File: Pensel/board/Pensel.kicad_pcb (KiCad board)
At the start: 2 copper layers, 60 x 13 mm, 62 parts, among them J3 JTAG, J4 I2C, J5 UART, P1 USB_PROC, SW2 MAIN, SW3 AUX, SW4 MODE_SEL, U1 STM32F302x6/8, U2 MMA8452Q, U3 MMA8452Q, U4 AP111733

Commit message: further improvements and new export of gerbers
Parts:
- removed the ? at (83.0, 141.1)
- removed the ? at (82.4, 140.5)
- removed the ? at (82.4, 141.1)
- added ?: via-1.0mm, TylerCustom:via-1.0mm, F.Cu at (58.5, 142.3)
- added ?: via-1.0mm, TylerCustom:via-1.0mm, F.Cu at (58.5, 140.8)
- added ?: via-1.0mm, TylerCustom:via-1.0mm, F.Cu at (82.5, 141.1)
- added ?: via-1.0mm, TylerCustom:via-1.0mm, F.Cu at (82.8, 141.1)
- added ?: via-1.0mm, TylerCustom:via-1.0mm, F.Cu at (81.5, 140.8)
- added ?: via-1.0mm, TylerCustom:via-1.0mm, F.Cu at (81.8, 140.8)
- added ?: via-1.0mm, TylerCustom:via-1.0mm, F.Cu at (82.2, 140.8)
- added ?: via-1.0mm, TylerCustom:via-1.0mm, F.Cu at (82.5, 140.8)
- added ?: via-1.0mm, TylerCustom:via-1.0mm, F.Cu at (53.6, 145.5)
- added ?: via-1.0mm, TylerCustom:via-1.0mm, F.Cu at (54.0, 145.5)
- added ?: via-1.0mm, TylerCustom:via-1.0mm, F.Cu at (54.0, 145.1)
- added ?: via-1.0mm, TylerCustom:via-1.0mm, F.Cu at (54.4, 145.1)
- added ?: via-1.0mm, TylerCustom:via-1.0mm, F.Cu at (58.5, 140.4)
- added ?: via-1.0mm, TylerCustom:via-1.0mm, F.Cu at (54.4, 145.5)
- added ?: via-1.0mm, TylerCustom:via-1.0mm, F.Cu at (63.5, 145.8)
- added ?: via-1.0mm, TylerCustom:via-1.0mm, F.Cu at (64.0, 145.8)
- added ?: via-1.0mm, TylerCustom:via-1.0mm, F.Cu at (64.0, 146.2)
- added ?: via-1.0mm, TylerCustom:via-1.0mm, F.Cu at (63.5, 146.2)
- added ?: via-1.0mm, TylerCustom:via-1.0mm, F.Cu at (63.0, 146.2)
- added ?: via-1.0mm, TylerCustom:via-1.0mm, F.Cu at (101.1, 139.8)
- added ?: via-1.0mm, TylerCustom:via-1.0mm, F.Cu at (101.1, 140.2)
- added ?: via-1.0mm, TylerCustom:via-1.0mm, F.Cu at (100.8, 140.2)
- added ?: via-1.0mm, TylerCustom:via-1.0mm, F.Cu at (101.5, 140.2)
- added ?: via-1.0mm, TylerCustom:via-1.0mm, F.Cu at (58.8, 140.4)
- added ?: via-1.0mm, TylerCustom:via-1.0mm, F.Cu at (102.0, 141.5)
- added ?: via-1.0mm, TylerCustom:via-1.0mm, F.Cu at (94.4, 143.3)
- added ?: via-1.0mm, TylerCustom:via-1.0mm, F.Cu at (104.4, 141.8)
- added ?: via-1.0mm, TylerCustom:via-1.0mm, F.Cu at (104.4, 142.3)
- added ?: via-1.0mm, TylerCustom:via-1.0mm, F.Cu at (104.4, 142.8)
- added ?: via-1.0mm, TylerCustom:via-1.0mm, F.Cu at (107.0, 149.5)
- added ?: via-1.0mm, TylerCustom:via-1.0mm, F.Cu at (107.6, 149.5)
- added ?: via-1.0mm, TylerCustom:via-1.0mm, F.Cu at (108.1, 149.5)
- added ?: via-1.0mm, TylerCustom:via-1.0mm, F.Cu at (108.7, 149.5)
- added ?: via-1.0mm, TylerCustom:via-1.0mm, F.Cu at (109.2, 149.5)
- added ?: via-1.0mm, TylerCustom:via-1.0mm, F.Cu at (65.4, 143.7)
- added ?: via-1.0mm, TylerCustom:via-1.0mm, F.Cu at (109.2, 149.9)
- added ?: via-1.0mm, TylerCustom:via-1.0mm, F.Cu at (109.2, 150.4)
- added ?: via-1.0mm, TylerCustom:via-1.0mm, F.Cu at (65.8, 143.3)
- added ?: via-1.0mm, TylerCustom:via-1.0mm, F.Cu at (66.1, 143.3)
- added ?: via-1.0mm, TylerCustom:via-1.0mm, F.Cu at (64.7, 143.3)
- added ?: via-1.0mm, TylerCustom:via-1.0mm, F.Cu at (64.7, 143.7)
- added ?: via-1.0mm, TylerCustom:via-1.0mm, F.Cu at (65.8, 143.7)
- added ?: via-1.0mm, TylerCustom:via-1.0mm, F.Cu at (64.3, 143.3)
- added ?: via-1.0mm, TylerCustom:via-1.0mm, F.Cu at (58.5, 141.2)
- added ?: via-1.0mm, TylerCustom:via-1.0mm, F.Cu at (64.3, 143.7)
- added ?: via-1.0mm, TylerCustom:via-1.0mm, F.Cu at (65.0, 143.7)
- added ?: via-1.0mm, TylerCustom:via-1.0mm, F.Cu at (65.0, 143.3)
- added ?: via-1.0mm, TylerCustom:via-1.0mm, F.Cu at (65.4, 143.3)
- added ?: via-1.0mm, TylerCustom:via-1.0mm, F.Cu at (66.1, 143.7)
- added ?: via-1.0mm, TylerCustom:via-1.0mm, F.Cu at (68.0, 140.1)
- added ?: via-1.0mm, TylerCustom:via-1.0mm, F.Cu at (68.0, 140.4)
- added ?: via-1.0mm, TylerCustom:via-1.0mm, F.Cu at (67.6, 140.1)
- added ?: via-1.0mm, TylerCustom:via-1.0mm, F.Cu at (67.6, 140.4)
- added ?: via-1.0mm, TylerCustom:via-1.0mm, F.Cu at (68.3, 140.4)
- added ?: via-1.0mm, TylerCustom:via-1.0mm, F.Cu at (58.5, 141.9)
- added ?: via-1.0mm, TylerCustom:via-1.0mm, F.Cu at (68.3, 140.1)
- added ?: via-1.0mm, TylerCustom:via-1.0mm, F.Cu at (66.8, 140.1)
- added ?: via-1.0mm, TylerCustom:via-1.0mm, F.Cu at (66.8, 140.4)
- added ?: via-1.0mm, TylerCustom:via-1.0mm, F.Cu at (67.2, 140.4)
- added ?: via-1.0mm, TylerCustom:via-1.0mm, F.Cu at (67.2, 140.1)
- added ?: via-1.0mm, TylerCustom:via-1.0mm, F.Cu at (66.5, 140.4)
- added ?: via-1.0mm, TylerCustom:via-1.0mm, F.Cu at (66.5, 140.1)
- added ?: via-1.0mm, TylerCustom:via-1.0mm, F.Cu at (73.8, 142.8)
- added ?: via-1.0mm, TylerCustom:via-1.0mm, F.Cu at (73.1, 142.1)
- added ?: via-1.0mm, TylerCustom:via-1.0mm, F.Cu at (73.5, 143.2)
- added ?: via-1.0mm, TylerCustom:via-1.0mm, F.Cu at (58.8, 141.9)
- added ?: via-1.0mm, TylerCustom:via-1.0mm, F.Cu at (73.8, 143.2)
- added ?: via-1.0mm, TylerCustom:via-1.0mm, F.Cu at (73.5, 142.1)
- added ?: via-1.0mm, TylerCustom:via-1.0mm, F.Cu at (73.8, 142.1)
- added ?: via-1.0mm, TylerCustom:via-1.0mm, F.Cu at (73.1, 143.2)
- added ?: via-1.0mm, TylerCustom:via-1.0mm, F.Cu at (73.8, 143.5)
- added ?: via-1.0mm, TylerCustom:via-1.0mm, F.Cu at (73.1, 143.5)
- added ?: via-1.0mm, TylerCustom:via-1.0mm, F.Cu at (73.5, 143.5)
- added ?: via-1.0mm, TylerCustom:via-1.0mm, F.Cu at (73.8, 142.4)
- added ?: via-1.0mm, TylerCustom:via-1.0mm, F.Cu at (73.1, 142.8)
- added ?: via-1.0mm, TylerCustom:via-1.0mm, F.Cu at (73.5, 142.8)
- added ?: via-1.0mm, TylerCustom:via-1.0mm, F.Cu at (58.8, 140.8)
- added ?: via-1.0mm, TylerCustom:via-1.0mm, F.Cu at (73.1, 142.4)
- added ?: via-1.0mm, TylerCustom:via-1.0mm, F.Cu at (73.5, 142.4)
- added ?: via-1.0mm, TylerCustom:via-1.0mm, F.Cu at (91.8, 143.8)
- added ?: via-1.0mm, TylerCustom:via-1.0mm, F.Cu at (98.9, 143.8)
- added ?: via-1.0mm, TylerCustom:via-1.0mm, F.Cu at (98.2, 143.8)
- added ?: via-1.0mm, TylerCustom:via-1.0mm, F.Cu at (98.9, 143.4)
- added ?: via-1.0mm, TylerCustom:via-1.0mm, F.Cu at (99.7, 143.4)
- added ?: via-1.0mm, TylerCustom:via-1.0mm, F.Cu at (98.2, 143.4)
- added ?: via-1.0mm, TylerCustom:via-1.0mm, F.Cu at (98.9, 143.1)
- added ?: via-1.0mm, TylerCustom:via-1.0mm, F.Cu at (99.7, 143.1)
- added ?: via-1.0mm, TylerCustom:via-1.0mm, F.Cu at (58.8, 141.6)
- added ?: via-1.0mm, TylerCustom:via-1.0mm, F.Cu at (98.2, 143.1)
- added ?: via-1.0mm, TylerCustom:via-1.0mm, F.Cu at (98.9, 142.8)
- added ?: via-1.0mm, TylerCustom:via-1.0mm, F.Cu at (99.7, 142.8)
- added ?: via-1.0mm, TylerCustom:via-1.0mm, F.Cu at (98.2, 142.8)
- added ?: via-1.0mm, TylerCustom:via-1.0mm, F.Cu at (98.9, 142.4)
- added ?: via-1.0mm, TylerCustom:via-1.0mm, F.Cu at (99.7, 142.4)
- added ?: via-1.0mm, TylerCustom:via-1.0mm, F.Cu at (98.2, 142.4)
- added ?: via-1.0mm, TylerCustom:via-1.0mm, F.Cu at (98.9, 142.1)
- added ?: via-1.0mm, TylerCustom:via-1.0mm, F.Cu at (99.7, 142.1)
- added ?: via-1.0mm, TylerCustom:via-1.0mm, F.Cu at (98.2, 142.1)
- added ?: via-1.0mm, TylerCustom:via-1.0mm, F.Cu at (58.8, 142.3)
- added ?: via-1.0mm, TylerCustom:via-1.0mm, F.Cu at (98.9, 141.7)
- added ?: via-1.0mm, TylerCustom:via-1.0mm, F.Cu at (99.7, 141.7)
- added ?: via-1.0mm, TylerCustom:via-1.0mm, F.Cu at (98.2, 141.7)
- added ?: via-1.0mm, TylerCustom:via-1.0mm, F.Cu at (98.9, 141.3)
- added ?: via-1.0mm, TylerCustom:via-1.0mm, F.Cu at (99.7, 141.3)
- added ?: via-1.0mm, TylerCustom:via-1.0mm, F.Cu at (98.2, 141.3)
- added ?: via-1.0mm, TylerCustom:via-1.0mm, F.Cu at (98.9, 141.0)
- added ?: via-1.0mm, TylerCustom:via-1.0mm, F.Cu at (99.7, 141.0)
- added ?: via-1.0mm, TylerCustom:via-1.0mm, F.Cu at (98.2, 141.0)
- added ?: via-1.0mm, TylerCustom:via-1.0mm, F.Cu at (98.9, 140.7)
- added ?: via-1.0mm, TylerCustom:via-1.0mm, F.Cu at (58.5, 141.6)
- added ?: via-1.0mm, TylerCustom:via-1.0mm, F.Cu at (99.7, 140.7)
- added ?: via-1.0mm, TylerCustom:via-1.0mm, F.Cu at (98.2, 140.7)
- added ?: via-1.0mm, TylerCustom:via-1.0mm, F.Cu at (81.5, 142.2)
- added ?: via-1.0mm, TylerCustom:via-1.0mm, F.Cu at (81.8, 142.2)
- added ?: via-1.0mm, TylerCustom:via-1.0mm, F.Cu at (82.2, 142.2)
- added ?: via-1.0mm, TylerCustom:via-1.0mm, F.Cu at (82.5, 142.2)
- added ?: via-1.0mm, TylerCustom:via-1.0mm, F.Cu at (82.8, 142.2)
- added ?: via-1.0mm, TylerCustom:via-1.0mm, F.Cu at (81.5, 141.8)
- added ?: via-1.0mm, TylerCustom:via-1.0mm, F.Cu at (81.8, 141.8)
- added ?: via-1.0mm, TylerCustom:via-1.0mm, F.Cu at (82.2, 141.8)
- added ?: via-1.0mm, TylerCustom:via-1.0mm, F.Cu at (58.8, 141.2)
- added ?: via-1.0mm, TylerCustom:via-1.0mm, F.Cu at (82.5, 141.8)
- added ?: via-1.0mm, TylerCustom:via-1.0mm, F.Cu at (82.8, 141.8)
- added ?: via-1.0mm, TylerCustom:via-1.0mm, F.Cu at (81.5, 141.4)
- added ?: via-1.0mm, TylerCustom:via-1.0mm, F.Cu at (81.8, 141.4)
- added ?: via-1.0mm, TylerCustom:via-1.0mm, F.Cu at (82.2, 141.4)
- added ?: via-1.0mm, TylerCustom:via-1.0mm, F.Cu at (82.5, 141.4)
- added ?: via-1.0mm, TylerCustom:via-1.0mm, F.Cu at (82.8, 141.4)
- added ?: via-1.0mm, TylerCustom:via-1.0mm, F.Cu at (81.5, 141.1)
- added ?: via-1.0mm, TylerCustom:via-1.0mm, F.Cu at (81.8, 141.1)
- added ?: via-1.0mm, TylerCustom:via-1.0mm, F.Cu at (82.2, 141.1)
- added REF**: Fiducial_1mm_Dia_2.54mm_Outer_CopperTop, Fiducials:Fiducial_1mm_Dia_2.54mm_Outer_CopperTop, B.Cu at (107.2, 139.7)
- added REF**: Fiducial_1mm_Dia_2.54mm_Outer_CopperTop, Fiducials:Fiducial_1mm_Dia_2.54mm_Outer_CopperTop, B.Cu at (52.0, 149.4)
- moved C10 8.43 mm to (107.8, 150.3), turned to 0 degrees
- moved ? 4.52 mm to (102.0, 141.0)
- moved ? 4.31 mm to (102.0, 142.0)
- moved ? 3.22 mm to (104.4, 141.4)
- moved C11 1.77 mm to (107.5, 146.0)
- moved C5 1.48 mm to (92.0, 141.9), turned to 270 degrees
- moved C7 1.48 mm to (90.8, 141.9), turned to 270 degrees
- moved ? 1.05 mm to (92.6, 143.8)
- moved REF** 0.78 mm to (103.4, 139.9)
- moved R3 0.71 mm to (95.5, 141.2), turned to 315 degrees
- moved ? 0.39 mm to (94.7, 143.6)
- moved R17 0.36 mm to (98.0, 147.1)
- moved ? 0.29 mm to (82.8, 140.8)
- moved ? 0.18 mm to (95.0, 143.9)
- moved ? 0.08 mm to (92.2, 143.5)
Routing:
- net +3V3: track 94.1 -> 90.1 mm, vias 19 -> 15
- net +5V: track 8.02 -> 9.43 mm
- net (no net): track 0.00 -> 0.70 mm
- net SWDIO: track 17.6 -> 17.0 mm
- net RESET_n: track 44.8 -> 44.2 mm
- net SWD-SWCLK: track 17.0 -> 16.3 mm
- net SWD-SWO: track 16.0 -> 15.4 mm
- net GND: track 68.2 -> 67.7 mm
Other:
- board text added: "1.0 3/17 Tyler Holmes"
- board text added: "GND"
- board text added: "I2C"
- board text added: "Pensel"
- board text added: "RX"
- board text added: "SCL"
- board text added: "SDA"
- board text added: "TX"
- board text added: "UART"

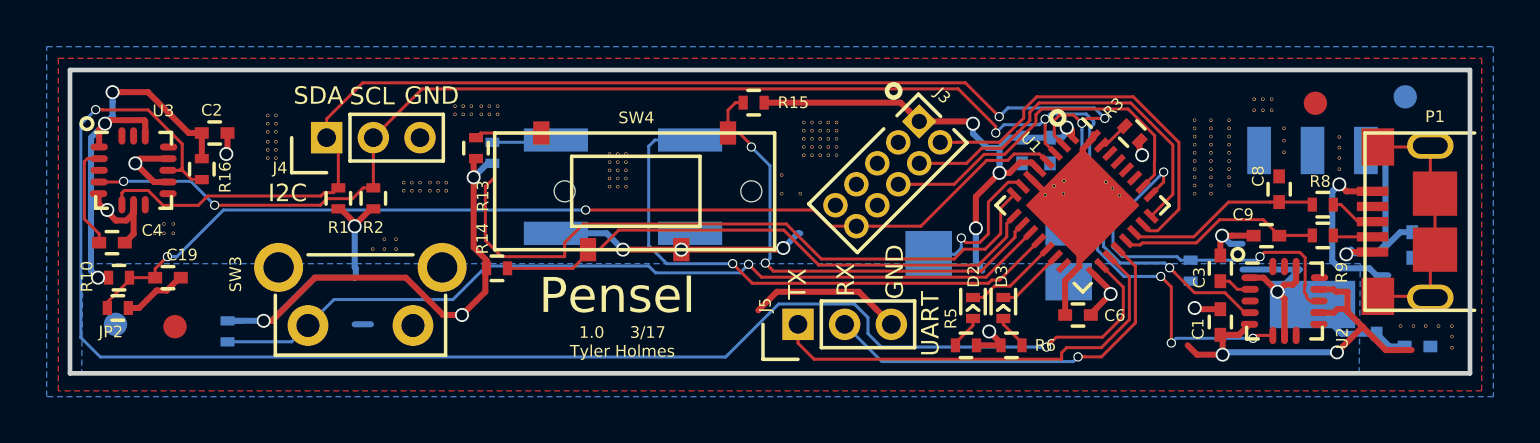
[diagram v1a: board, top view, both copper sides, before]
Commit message: switched to LSM303DLHC accel and gyro only and did first cut at ull route
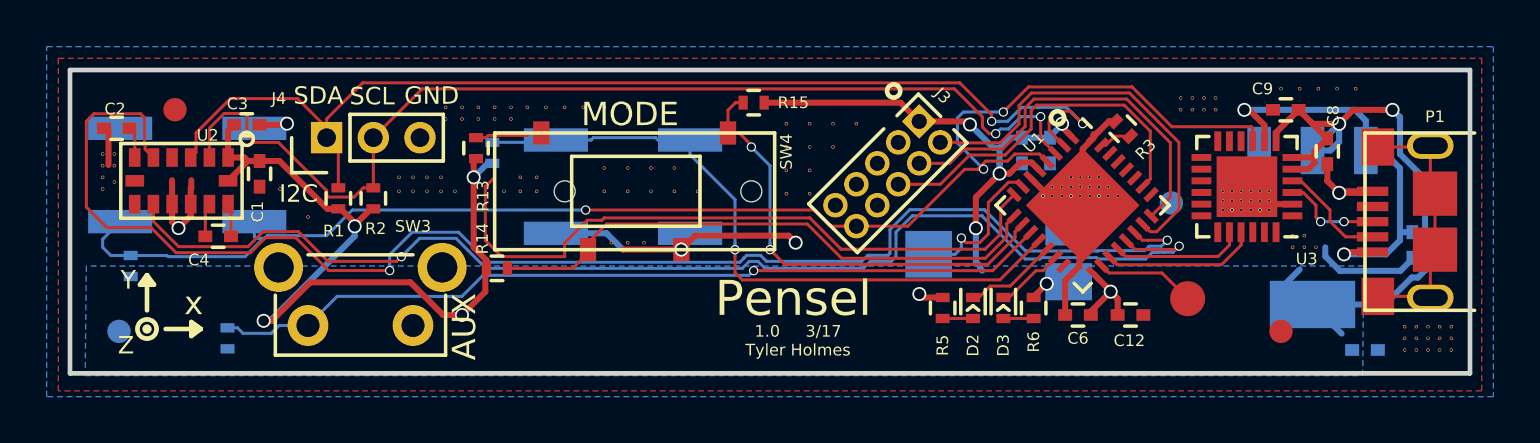
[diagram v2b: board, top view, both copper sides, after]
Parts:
- removed the ? at (58.5, 142.3)
- removed the ? at (58.5, 140.8)
- removed the ? at (82.5, 141.1)
- removed the ? at (82.8, 141.1)
- removed the ? at (81.5, 140.8)
- removed the ? at (81.8, 140.8)
- removed the ? at (82.2, 140.8)
- removed the ? at (82.5, 140.8)
- removed the ? at (53.6, 145.5)
- removed the ? at (54.0, 145.5)
- removed the ? at (54.0, 145.1)
- removed the ? at (54.4, 145.1)
- removed the ? at (58.5, 140.4)
- removed the ? at (54.4, 145.5)
- removed the ? at (63.5, 145.8)
- removed the ? at (64.0, 145.8)
- removed the ? at (64.0, 146.2)
- removed the ? at (63.5, 146.2)
- removed the ? at (63.0, 146.2)
- removed the ? at (101.1, 139.8)
- removed the ? at (101.1, 140.2)
- removed the ? at (100.8, 140.2)
- removed the ? at (101.5, 140.2)
- removed the ? at (58.8, 140.4)
- removed the ? at (102.0, 141.5)
- removed the ? at (94.4, 143.3)
- removed the ? at (104.4, 141.8)
- removed the ? at (104.4, 142.3)
- removed the ? at (104.4, 142.8)
- removed the ? at (107.0, 149.5)
- removed the ? at (107.6, 149.5)
- removed the ? at (108.1, 149.5)
- removed the ? at (108.7, 149.5)
- removed the ? at (109.2, 149.5)
- removed the ? at (65.4, 143.7)
- removed the ? at (109.2, 149.9)
- removed the ? at (109.2, 150.4)
- removed the ? at (94.7, 143.6)
- removed the ? at (82.8, 140.8)
- removed the ? at (95.0, 143.9)
- removed the ? at (104.4, 141.4)
- removed the ? at (101.5, 139.8)
- removed the ? at (100.8, 139.8)
- removed the ? at (81.3, 143.8)
- removed the ? at (80.5, 143.0)
- removed the ? at (65.8, 143.3)
- removed the ? at (80.5, 143.8)
- removed the ? at (92.6, 143.8)
- removed the ? at (92.6, 143.2)
- removed the ? at (92.2, 143.5)
- removed the ? at (102.0, 141.0)
- removed the ? at (102.0, 142.0)
- removed the ? at (66.1, 143.3)
- removed the ? at (64.7, 143.3)
- removed the ? at (64.7, 143.7)
- removed the ? at (65.8, 143.7)
- removed the ? at (64.3, 143.3)
- removed the ? at (58.5, 141.2)
- removed the ? at (64.3, 143.7)
- removed the ? at (65.0, 143.7)
- removed the ? at (65.0, 143.3)
- removed the ? at (65.4, 143.3)
- removed the ? at (66.1, 143.7)
- removed the ? at (68.0, 140.1)
- removed the ? at (68.0, 140.4)
- removed the ? at (67.6, 140.1)
- removed the ? at (67.6, 140.4)
- removed the ? at (68.3, 140.4)
- removed the ? at (58.5, 141.9)
- removed the ? at (68.3, 140.1)
- removed the ? at (66.8, 140.1)
- removed the ? at (66.8, 140.4)
- removed the ? at (67.2, 140.4)
- removed the ? at (67.2, 140.1)
- removed the ? at (66.5, 140.4)
- removed the ? at (66.5, 140.1)
- removed the ? at (73.8, 142.8)
- removed the ? at (73.1, 142.1)
- removed the ? at (73.5, 143.2)
- removed the ? at (58.8, 141.9)
- removed the ? at (73.8, 143.2)
- removed the ? at (73.5, 142.1)
- removed the ? at (73.8, 142.1)
- removed the ? at (73.1, 143.2)
- removed the ? at (73.8, 143.5)
- removed the ? at (73.1, 143.5)
- removed the ? at (73.5, 143.5)
- removed the ? at (73.8, 142.4)
- removed the ? at (73.1, 142.8)
- removed the ? at (73.5, 142.8)
- removed the ? at (58.8, 140.8)
- removed the ? at (73.1, 142.4)
- removed the ? at (73.5, 142.4)
- removed the ? at (91.8, 143.8)
- removed the ? at (98.9, 143.8)
- removed the ? at (98.2, 143.8)
- removed the ? at (98.9, 143.4)
- removed the ? at (99.7, 143.4)
- removed the ? at (98.2, 143.4)
- removed the ? at (98.9, 143.1)
- removed the ? at (99.7, 143.1)
- removed the ? at (58.8, 141.6)
- removed the ? at (98.2, 143.1)
- removed the ? at (98.9, 142.8)
- removed the ? at (99.7, 142.8)
- removed the ? at (98.2, 142.8)
- removed the ? at (98.9, 142.4)
- removed the ? at (99.7, 142.4)
- removed the ? at (98.2, 142.4)
- removed the ? at (98.9, 142.1)
- removed the ? at (99.7, 142.1)
- removed the ? at (98.2, 142.1)
- removed the ? at (58.8, 142.3)
- removed the ? at (98.9, 141.7)
- removed the ? at (99.7, 141.7)
- removed the ? at (98.2, 141.7)
- removed the ? at (98.9, 141.3)
- removed the ? at (99.7, 141.3)
- removed the ? at (98.2, 141.3)
- removed the ? at (98.9, 141.0)
- removed the ? at (99.7, 141.0)
- removed the ? at (98.2, 141.0)
- removed the ? at (98.9, 140.7)
- removed the ? at (58.5, 141.6)
- removed the ? at (99.7, 140.7)
- removed the ? at (98.2, 140.7)
- removed the ? at (81.5, 142.2)
- removed the ? at (81.8, 142.2)
- removed the ? at (82.2, 142.2)
- removed the ? at (82.5, 142.2)
- removed the ? at (82.8, 142.2)
- removed the ? at (81.5, 141.8)
- removed the ? at (81.8, 141.8)
- removed the ? at (82.2, 141.8)
- removed the ? at (58.8, 141.2)
- removed the ? at (82.5, 141.8)
- removed the ? at (82.8, 141.8)
- removed the ? at (81.5, 141.4)
- removed the ? at (81.8, 141.4)
- removed the ? at (82.2, 141.4)
- removed the ? at (82.5, 141.4)
- removed the ? at (82.8, 141.4)
- removed the ? at (81.5, 141.1)
- removed the ? at (81.8, 141.1)
- removed the ? at (82.2, 141.1)
- removed C15, C19: 0.1 uF, Capacitors_SMD:C_0402
- removed JP2: JMPR, Resistors_SMD:R_0402
- removed R16, R17: 4K7, Resistors_SMD:R_0402
- removed R8, R9: 27R, Resistors_SMD:R_0402
- removed REF** (x4): Fiducial_1mm_Dia_2.54mm_Outer_CopperTop, Fiducials:Fiducial_1mm_Dia_2.54mm_Outer_CopperTop
- added ?: via-1.0mm, TylerCustom:via-1.0mm, F.Cu at (83.7, 140.8)
- added ?: via-1.0mm, TylerCustom:via-1.0mm, F.Cu at (66.8, 140.1)
- added ?: via-1.0mm, TylerCustom:via-1.0mm, F.Cu at (92.5, 143.5)
- added ?: via-1.0mm, TylerCustom:via-1.0mm, F.Cu at (92.9, 143.5)
- added ?: via-1.0mm, TylerCustom:via-1.0mm, F.Cu at (93.3, 143.5)
- added ?: via-1.0mm, TylerCustom:via-1.0mm, F.Cu at (93.7, 143.5)
- added ?: via-1.0mm, TylerCustom:via-1.0mm, F.Cu at (94.1, 143.5)
- added ?: via-1.0mm, TylerCustom:via-1.0mm, F.Cu at (94.5, 143.5)
- added ?: via-1.0mm, TylerCustom:via-1.0mm, F.Cu at (94.9, 143.9)
- added ?: via-1.0mm, TylerCustom:via-1.0mm, F.Cu at (94.5, 143.9)
- added ?: via-1.0mm, TylerCustom:via-1.0mm, F.Cu at (94.1, 143.9)
- added ?: via-1.0mm, TylerCustom:via-1.0mm, F.Cu at (93.7, 143.9)
- added ?: via-1.0mm, TylerCustom:via-1.0mm, F.Cu at (67.5, 140.1)
- added ?: via-1.0mm, TylerCustom:via-1.0mm, F.Cu at (93.3, 143.9)
- added ?: via-1.0mm, TylerCustom:via-1.0mm, F.Cu at (92.9, 143.9)
- added ?: via-1.0mm, TylerCustom:via-1.0mm, F.Cu at (92.5, 143.9)
- added ?: via-1.0mm, TylerCustom:via-1.0mm, F.Cu at (92.1, 143.9)
- added ?: via-1.0mm, TylerCustom:via-1.0mm, F.Cu at (91.7, 143.9)
- added ?: via-1.0mm, TylerCustom:via-1.0mm, F.Cu at (101.4, 143.7)
- added ?: via-1.0mm, TylerCustom:via-1.0mm, F.Cu at (101.0, 143.7)
- added ?: via-1.0mm, TylerCustom:via-1.0mm, F.Cu at (100.6, 143.7)
- added ?: via-1.0mm, TylerCustom:via-1.0mm, F.Cu at (100.2, 143.7)
- added ?: via-1.0mm, TylerCustom:via-1.0mm, F.Cu at (99.8, 143.7)
- added ?: via-1.0mm, TylerCustom:via-1.0mm, F.Cu at (68.2, 140.1)
- added ?: via-1.0mm, TylerCustom:via-1.0mm, F.Cu at (99.4, 143.7)
- added ?: via-1.0mm, TylerCustom:via-1.0mm, F.Cu at (99.4, 144.1)
- added ?: via-1.0mm, TylerCustom:via-1.0mm, F.Cu at (99.8, 144.1)
- added ?: via-1.0mm, TylerCustom:via-1.0mm, F.Cu at (100.2, 144.1)
- added ?: via-1.0mm, TylerCustom:via-1.0mm, F.Cu at (100.6, 144.1)
- added ?: via-1.0mm, TylerCustom:via-1.0mm, F.Cu at (101.0, 144.1)
- added ?: via-1.0mm, TylerCustom:via-1.0mm, F.Cu at (101.4, 144.1)
- added ?: via-1.0mm, TylerCustom:via-1.0mm, F.Cu at (101.4, 144.5)
- added ?: via-1.0mm, TylerCustom:via-1.0mm, F.Cu at (101.0, 144.5)
- added ?: via-1.0mm, TylerCustom:via-1.0mm, F.Cu at (100.6, 144.5)
- added ?: via-1.0mm, TylerCustom:via-1.0mm, F.Cu at (68.9, 140.1)
- added ?: via-1.0mm, TylerCustom:via-1.0mm, F.Cu at (100.2, 144.5)
- added ?: via-1.0mm, TylerCustom:via-1.0mm, F.Cu at (99.8, 144.5)
- added ?: via-1.0mm, TylerCustom:via-1.0mm, F.Cu at (99.4, 144.5)
- added ?: via-1.0mm, TylerCustom:via-1.0mm, F.Cu at (109.2, 149.5)
- added ?: via-1.0mm, TylerCustom:via-1.0mm, B.Cu at (108.7, 149.5)
- added ?: via-1.0mm, TylerCustom:via-1.0mm, F.Cu at (108.2, 149.5)
- added ?: via-1.0mm, TylerCustom:via-1.0mm, F.Cu at (69.6, 140.1)
- added ?: via-1.0mm, TylerCustom:via-1.0mm, F.Cu at (70.4, 140.1)
- added ?: via-1.0mm, TylerCustom:via-1.0mm, F.Cu at (71.2, 140.1)
- added ?: via-1.0mm, TylerCustom:via-1.0mm, F.Cu at (72.0, 140.1)
- added ?: via-1.0mm, TylerCustom:via-1.0mm, F.Cu at (70.0, 143.1)
- added ?: via-1.0mm, TylerCustom:via-1.0mm, F.Cu at (69.3, 143.1)
- added ?: via-1.0mm, TylerCustom:via-1.0mm, F.Cu at (82.7, 140.8)
- added ?: via-1.0mm, TylerCustom:via-1.0mm, F.Cu at (68.6, 143.7)
- added ?: via-1.0mm, TylerCustom:via-1.0mm, F.Cu at (69.3, 143.7)
- added ?: via-1.0mm, TylerCustom:via-1.0mm, F.Cu at (70.0, 143.7)
- added ?: via-1.0mm, TylerCustom:via-1.0mm, F.Cu at (59.0, 143.6)
- added ?: via-1.0mm, TylerCustom:via-1.0mm, F.Cu at (64.1, 143.1)
- added ?: via-1.0mm, TylerCustom:via-1.0mm, F.Cu at (64.7, 143.1)
- added ?: via-1.0mm, TylerCustom:via-1.0mm, F.Cu at (65.3, 143.1)
- added ?: via-1.0mm, TylerCustom:via-1.0mm, F.Cu at (65.9, 143.1)
- added ?: via-1.0mm, TylerCustom:via-1.0mm, F.Cu at (66.5, 143.7)
- added ?: via-1.0mm, TylerCustom:via-1.0mm, F.Cu at (65.9, 143.7)
- added ?: via-1.0mm, TylerCustom:via-1.0mm, F.Cu at (82.7, 141.8)
- added ?: via-1.0mm, TylerCustom:via-1.0mm, F.Cu at (65.3, 143.7)
- added ?: via-1.0mm, TylerCustom:via-1.0mm, F.Cu at (64.7, 143.7)
- added ?: via-1.0mm, TylerCustom:via-1.0mm, F.Cu at (64.1, 143.7)
- added ?: via-1.0mm, TylerCustom:via-1.0mm, F.Cu at (74.6, 145.9)
- added ?: via-1.0mm, TylerCustom:via-1.0mm, F.Cu at (73.9, 145.9)
- added ?: via-1.0mm, TylerCustom:via-1.0mm, F.Cu at (73.2, 145.9)
- added ?: via-1.0mm, TylerCustom:via-1.0mm, F.Cu at (105.1, 139.3)
- added ?: via-1.0mm, TylerCustom:via-1.0mm, F.Cu at (102.9, 145.6)
- added ?: via-1.0mm, TylerCustom:via-1.0mm, F.Cu at (102.4, 145.6)
- added ?: via-1.0mm, TylerCustom:via-1.0mm, F.Cu at (102.4, 146.1)
- added ?: via-1.0mm, TylerCustom:via-1.0mm, F.Cu at (68.9, 140.6)
- added ?: via-1.0mm, TylerCustom:via-1.0mm, F.Cu at (102.9, 146.1)
- added ?: via-1.0mm, TylerCustom:via-1.0mm, F.Cu at (103.4, 146.1)
- added ?: via-1.0mm, TylerCustom:via-1.0mm, F.Cu at (107.2, 150.5)
- added ?: via-1.0mm, TylerCustom:via-1.0mm, F.Cu at (107.7, 150.5)
- added ?: via-1.0mm, TylerCustom:via-1.0mm, F.Cu at (108.2, 150.5)
- added ?: via-1.0mm, TylerCustom:via-1.0mm, F.Cu at (108.7, 150.5)
- added ?: via-1.0mm, TylerCustom:via-1.0mm, F.Cu at (109.2, 150.5)
- added ?: via-1.0mm, TylerCustom:via-1.0mm, F.Cu at (109.2, 150.0)
- added ?: via-1.0mm, TylerCustom:via-1.0mm, F.Cu at (108.7, 150.0)
- added ?: via-1.0mm, TylerCustom:via-1.0mm, F.Cu at (108.2, 150.0)
- added ?: via-1.0mm, TylerCustom:via-1.0mm, F.Cu at (68.2, 140.6)
- added ?: via-1.0mm, TylerCustom:via-1.0mm, F.Cu at (107.7, 150.0)
- added ?: via-1.0mm, TylerCustom:via-1.0mm, F.Cu at (107.2, 150.0)
- added ?: via-1.0mm, TylerCustom:via-1.0mm, F.Cu at (107.2, 149.5)
- added ?: via-1.0mm, TylerCustom:via-1.0mm, F.Cu at (107.7, 149.5)
- added ?: via-1.0mm, TylerCustom:via-1.0mm, F.Cu at (73.9, 140.1)
- added ?: via-1.0mm, TylerCustom:via-1.0mm, F.Cu at (72.9, 140.1)
- added ?: via-1.0mm, TylerCustom:via-1.0mm, F.Cu at (73.9, 140.7)
- added ?: via-1.0mm, TylerCustom:via-1.0mm, F.Cu at (81.7, 140.8)
- added ?: via-1.0mm, TylerCustom:via-1.0mm, F.Cu at (80.7, 140.8)
- added ?: via-1.0mm, TylerCustom:via-1.0mm, F.Cu at (81.7, 141.8)
- added ?: via-1.0mm, TylerCustom:via-1.0mm, F.Cu at (67.5, 140.6)
- added ?: via-1.0mm, TylerCustom:via-1.0mm, F.Cu at (80.7, 141.8)
- added ?: via-1.0mm, TylerCustom:via-1.0mm, F.Cu at (81.7, 142.8)
- added ?: via-1.0mm, TylerCustom:via-1.0mm, F.Cu at (80.7, 142.8)
- added ?: via-1.0mm, TylerCustom:via-1.0mm, F.Cu at (81.7, 143.8)
- added ?: via-1.0mm, TylerCustom:via-1.0mm, F.Cu at (80.7, 143.8)
- added ?: via-1.0mm, TylerCustom:via-1.0mm, F.Cu at (72.9, 143.7)
- added ?: via-1.0mm, TylerCustom:via-1.0mm, F.Cu at (72.9, 140.7)
- added ?: via-1.0mm, TylerCustom:via-1.0mm, F.Cu at (75.9, 142.7)
- added ?: via-1.0mm, TylerCustom:via-1.0mm, F.Cu at (74.9, 142.7)
- added ?: via-1.0mm, TylerCustom:via-1.0mm, F.Cu at (73.9, 142.7)
- added ?: via-1.0mm, TylerCustom:via-1.0mm, F.Cu at (66.8, 140.6)
- added ?: via-1.0mm, TylerCustom:via-1.0mm, F.Cu at (72.9, 142.7)
- added ?: via-1.0mm, TylerCustom:via-1.0mm, F.Cu at (76.9, 143.7)
- added ?: via-1.0mm, TylerCustom:via-1.0mm, F.Cu at (75.9, 143.7)
- added ?: via-1.0mm, TylerCustom:via-1.0mm, F.Cu at (74.9, 143.7)
- added ?: via-1.0mm, TylerCustom:via-1.0mm, F.Cu at (73.9, 143.7)
- added ?: via-1.0mm, TylerCustom:via-1.0mm, F.Cu at (51.9, 143.3)
- added ?: via-1.0mm, TylerCustom:via-1.0mm, F.Cu at (51.9, 142.6)
- added ?: via-1.0mm, TylerCustom:via-1.0mm, F.Cu at (51.9, 142.1)
- added ?: via-1.0mm, TylerCustom:via-1.0mm, F.Cu at (51.4, 142.1)
- added ?: via-1.0mm, TylerCustom:via-1.0mm, F.Cu at (51.4, 142.6)
- added ?: via-1.0mm, TylerCustom:via-1.0mm, F.Cu at (66.1, 140.6)
- added ?: via-1.0mm, TylerCustom:via-1.0mm, F.Cu at (51.4, 143.1)
- added ?: via-1.0mm, TylerCustom:via-1.0mm, F.Cu at (51.4, 143.6)
- added ?: via-1.0mm, TylerCustom:via-1.0mm, F.Cu at (60.2, 144.8)
- added ?: via-1.0mm, TylerCustom:via-1.0mm, F.Cu at (97.6, 139.7)
- added ?: via-1.0mm, TylerCustom:via-1.0mm, F.Cu at (98.1, 139.7)
- added ?: via-1.0mm, TylerCustom:via-1.0mm, F.Cu at (98.6, 139.7)
- added ?: via-1.0mm, TylerCustom:via-1.0mm, F.Cu at (99.1, 139.7)
- added ?: via-1.0mm, TylerCustom:via-1.0mm, F.Cu at (99.1, 140.2)
- added ?: via-1.0mm, TylerCustom:via-1.0mm, F.Cu at (98.6, 140.2)
- added ?: via-1.0mm, TylerCustom:via-1.0mm, F.Cu at (98.1, 140.2)
- added ?: via-1.0mm, TylerCustom:via-1.0mm, F.Cu at (66.1, 140.1)
- added ?: via-1.0mm, TylerCustom:via-1.0mm, F.Cu at (97.6, 140.2)
- added ?: via-1.0mm, TylerCustom:via-1.0mm, F.Cu at (104.3, 139.3)
- added ?: via-1.0mm, TylerCustom:via-1.0mm, F.Cu at (103.5, 139.3)
- added ?: via-1.0mm, TylerCustom:via-1.0mm, F.Cu at (102.7, 139.3)
- added ?: via-1.0mm, TylerCustom:via-1.0mm, F.Cu at (101.9, 139.3)
- added ?: via-1.0mm, TylerCustom:via-1.0mm, F.Cu at (94.1, 143.1)
- added ?: via-1.0mm, TylerCustom:via-1.0mm, F.Cu at (93.7, 143.1)
- added ?: via-1.0mm, TylerCustom:via-1.0mm, F.Cu at (93.3, 143.1)
- added ?: via-1.0mm, TylerCustom:via-1.0mm, F.Cu at (92.9, 143.1)
- added ?: via-1.0mm, TylerCustom:via-1.0mm, F.Cu at (92.1, 143.5)
- added C12: 0.1 uF, Capacitors_SMD:C_0402, F.Cu at (95.5, 149.0)
- added J1: TEST_1P, Measurement_Points:Measurement_Point_Round-SMD-Pad_Small, F.Cu at (97.9, 148.3)
- added J2: Fiducial, Fiducials:Fiducial_1mm_Dia_2.54mm_Outer_CopperBottom, F.Cu at (97.2, 144.2)
- added J6: Fiducial, Fiducials:Fiducial_1mm_Dia_2.54mm_Outer_CopperTop, F.Cu at (54.5, 140.2)
- added J7: Fiducial, Fiducials:Fiducial_1mm_Dia_2.54mm_Outer_CopperTop, F.Cu at (101.9, 149.7)
- added SW1: RST, Buttons_Switches_SMD:SW_SPST_B3SL-1002P, B.Cu at (55.0, 143.0)
- C4: value 0.1 uF -> 0.22 uF
- C8: value 47 pF -> 4.7 uF
- C9: value 47 pF -> 0.1 uF
- J5: value UART -> Fiducial; footprint Pin_Headers:Pin_Header_Straight_1x03_Pitch2.00mm -> Fiducials:Fiducial_1mm_Dia_2.54mm_Outer_CopperBottom
- R10: moved to B.Cu
- U2: value MMA8452Q -> LSM303DLHC; footprint TylerCustom:QFN-16_3x3mm_Pitch0.5mm_5x3pin -> TylerCustom:LGA_14L_3mm_5mm
- U3: value MMA8452Q -> CP2102N-A01-GQFN24; footprint TylerCustom:QFN-16_3x3mm_Pitch0.5mm_5x3pin -> Housings_DFN_QFN:QFN-24-1EP_4x4mm_Pitch0.5mm
- moved U3 47.7 mm to (100.4, 143.5), turned to 180 degrees
- moved U2 47.6 mm to (54.8, 143.2)
- moved C3 42.2 mm to (57.6, 140.8), turned to 0 degrees
- moved C1 41.7 mm to (58.1, 142.9)
- moved J5 29.1 mm to (52.1, 149.7), turned to 0 degrees
- moved C9 5.46 mm to (102.1, 140.2)
- moved C4 4.56 mm to (56.4, 145.6), turned to 180 degrees
- moved C2 4.20 mm to (52.0, 141.0), turned to 180 degrees
- moved C8 2.63 mm to (103.9, 142.0)
- moved C10 2.25 mm to (105.5, 150.5)
- moved R5 1.89 mm to (87.4, 148.7), turned to 270 degrees
- moved R6 1.86 mm to (91.3, 148.7), turned to 270 degrees
- moved R10 0.71 mm to (52.6, 146.9), turned to 90 degrees
- moved R3 0.46 mm to (95.1, 141.0), turned to 135 degrees
- moved R12 0.30 mm to (56.8, 150.0), turned to 90 degrees
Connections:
- C2 pad 1: +3V3 -> Net-(C2-Pad1)
- C3 pad 1: Net-(C3-Pad1) -> +3V3
- C4 pad 2: GND -> Net-(C4-Pad2)
- C8 pad 1: GND -> +3V3
- C8 pad 2: USB_DP -> GND
- C9 pad 1: USB_DN -> +3V3
- J3 pad 7: (no net) -> Net-(J3-Pad7)
- J3 pad 8: (no net) -> Net-(J3-Pad8)
- P1 pad 4: (no net) -> Net-(P1-Pad4)
- U1 pad 15: (no net) -> Net-(U1-Pad15)
- U1 pad 18: ACCEL_INT1_BTM -> Net-(J1-Pad1)
- U1 pad 21: USB_DN -> SEN_DRDY
- U1 pad 22: USB_DP -> SEN_INT1
- U1 pad 25: ACCEL_INT1_TOP -> Net-(U1-Pad25)
- U1 pad 27: (no net) -> Net-(U1-Pad27)
- U1 pad 28: (no net) -> Net-(U1-Pad28)
- U1 pad 29: (no net) -> Net-(U1-Pad29)
- U1 pad 30: (no net) -> Net-(U1-Pad30)
- U2 pad 11: ACCEL_INT1_TOP -> GND
- U2 pad 12: GND -> Net-(C4-Pad2)
- U2 pad 13: (no net) -> Net-(C4-Pad1)
- U2 pad 2: Net-(C3-Pad1) -> SCL
- U2 pad 3: (no net) -> SDA
- U2 pad 4: SCL -> Net-(U2-Pad4)
- U2 pad 5: GND -> SEN_INT1
- U2 pad 6: SDA -> Net-(C2-Pad1)
- U2 pad 7: +3V3 -> GND
- U2 pad 8: (no net) -> Net-(U2-Pad8)
- U2 pad 9: (no net) -> SEN_DRDY
- U3 pad 1: +3V3 -> Net-(U3-Pad1)
- U3 pad 10: GND -> Net-(U3-Pad10)
- U3 pad 11: ACCEL_INT1_BTM -> Net-(U3-Pad11)
- U3 pad 12: GND -> Net-(U3-Pad12)
- U3 pad 13: (no net) -> Net-(U3-Pad13)
- U3 pad 14: +3V3 -> Net-(U3-Pad14)
- U3 pad 15: (no net) -> Net-(U3-Pad15)
- U3 pad 16: (no net) -> Net-(U3-Pad16)
- U3 pad 2: Net-(C4-Pad1) -> GND
- U3 pad 3: (no net) -> Net-(P1-Pad3)
- U3 pad 4: SCL -> Net-(P1-Pad2)
- U3 pad 5: GND -> +3V3
- U3 pad 6: SDA -> +3V3
- U3 pad 7: GND -> +3V3
- U3 pad 8: (no net) -> +5V
- U3 pad 9: (no net) -> RESET_n
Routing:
- net ACCEL_INT1_BTM: track 67.4 -> 0.00 mm, vias 2 -> 0
- net SEN_INT1: track 0.00 -> 62.3 mm, vias 0 -> 2
- net SEN_DRDY: track 0.00 -> 52.6 mm, vias 0 -> 2
- net GND: track 67.7 -> 39.5 mm, vias 11 -> 5
- net SDA: track 68.6 -> 49.1 mm, vias 6 -> 2
- net RESET_n: track 44.2 -> 63.1 mm, vias 2 -> 3
- net SCL: track 62.6 -> 45.6 mm, vias 5 -> 2
- net ACCEL_INT1_TOP: track 16.4 -> 0.00 mm, vias 2 -> 0
- net DBG_UART_TX: track 19.2 -> 6.66 mm
- net DBG_UART_RX: track 17.3 -> 5.66 mm, vias 1 -> 0
- net USB_DN: track 8.85 -> 0.00 mm
- net +5V: track 9.43 -> 17.9 mm, vias 1 -> 2
- net USB_DP: track 8.35 -> 0.00 mm
- net Net-(J1-Pad1): track 0.00 -> 4.27 mm
- net Net-(P1-Pad2): track 1.71 -> 4.71 mm
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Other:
- board text added: "AUX"
- board text added: "MAIN"
- board text added: "MODE"
- board text added: "RST"
- board text added: "SENSITIVITY"
- board text added: "Y"
- board text added: "Z"
- board text added: "x"
- board text removed: "RX"
- board text removed: "TX"
- board text removed: "UART"
